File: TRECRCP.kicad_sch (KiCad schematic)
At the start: 44 parts, among them K1 12v Coil Relay, K2 12v Coil Relay, K5 Fujitsu_FTR-LYCA005x, K6 Fujitsu_FTR-LYCA005x, K7 Fujitsu_FTR-LYCA005x, Q2 STF40NF03L, Q3 STF40NF03L, Q4 STF40NF03L, SW1 Dispatch2, SW1 Maint/Off/On Switch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

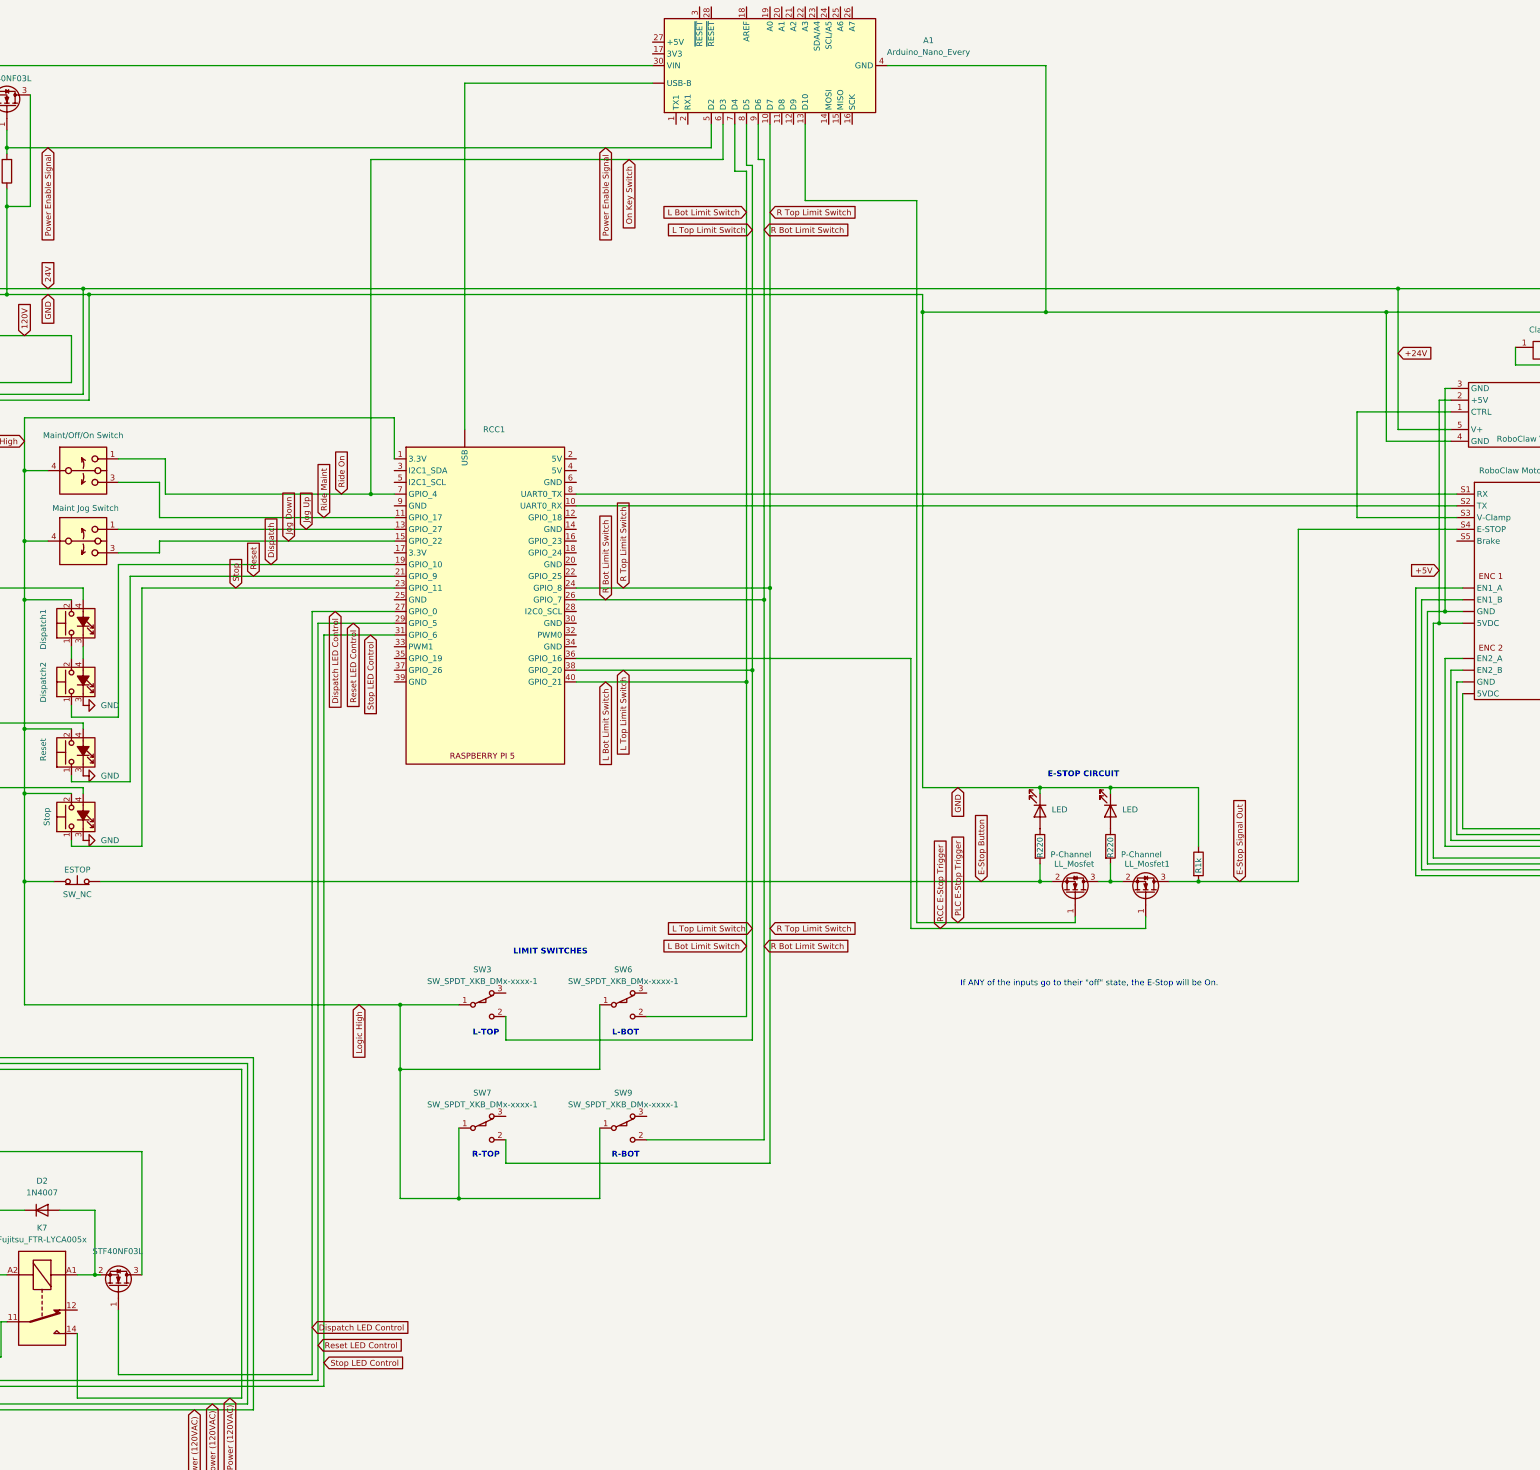
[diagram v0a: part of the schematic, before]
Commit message: Add Pi PSU
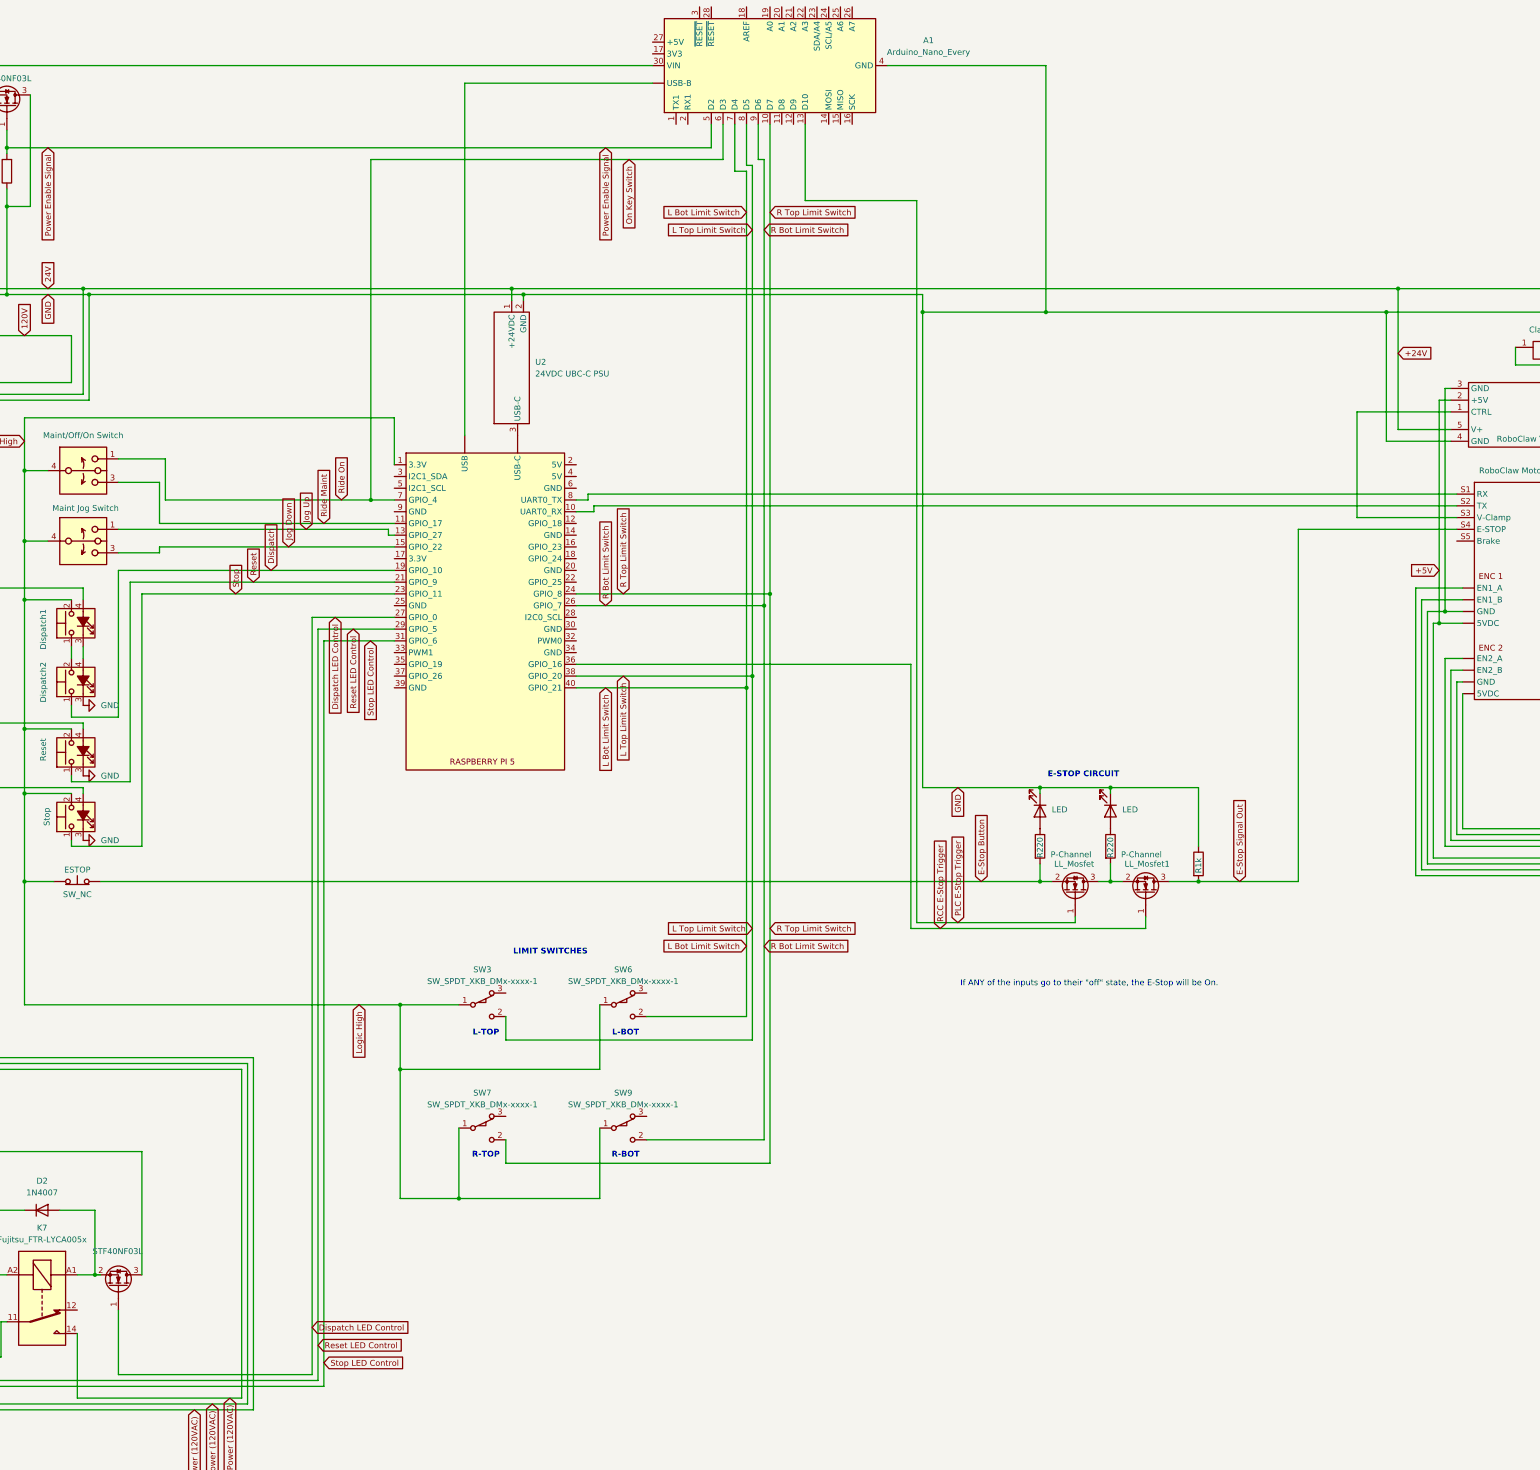
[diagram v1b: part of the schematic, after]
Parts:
- added U2: 24VDC UBC-C PSU, symbol custom symbols:Pi_PSU
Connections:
- net +24V: now also U2.1 (+24VDC)
- net GND: now also U2.2 (GND)
- new net: RCC1. (USB-C), U2.3 (USB-C)

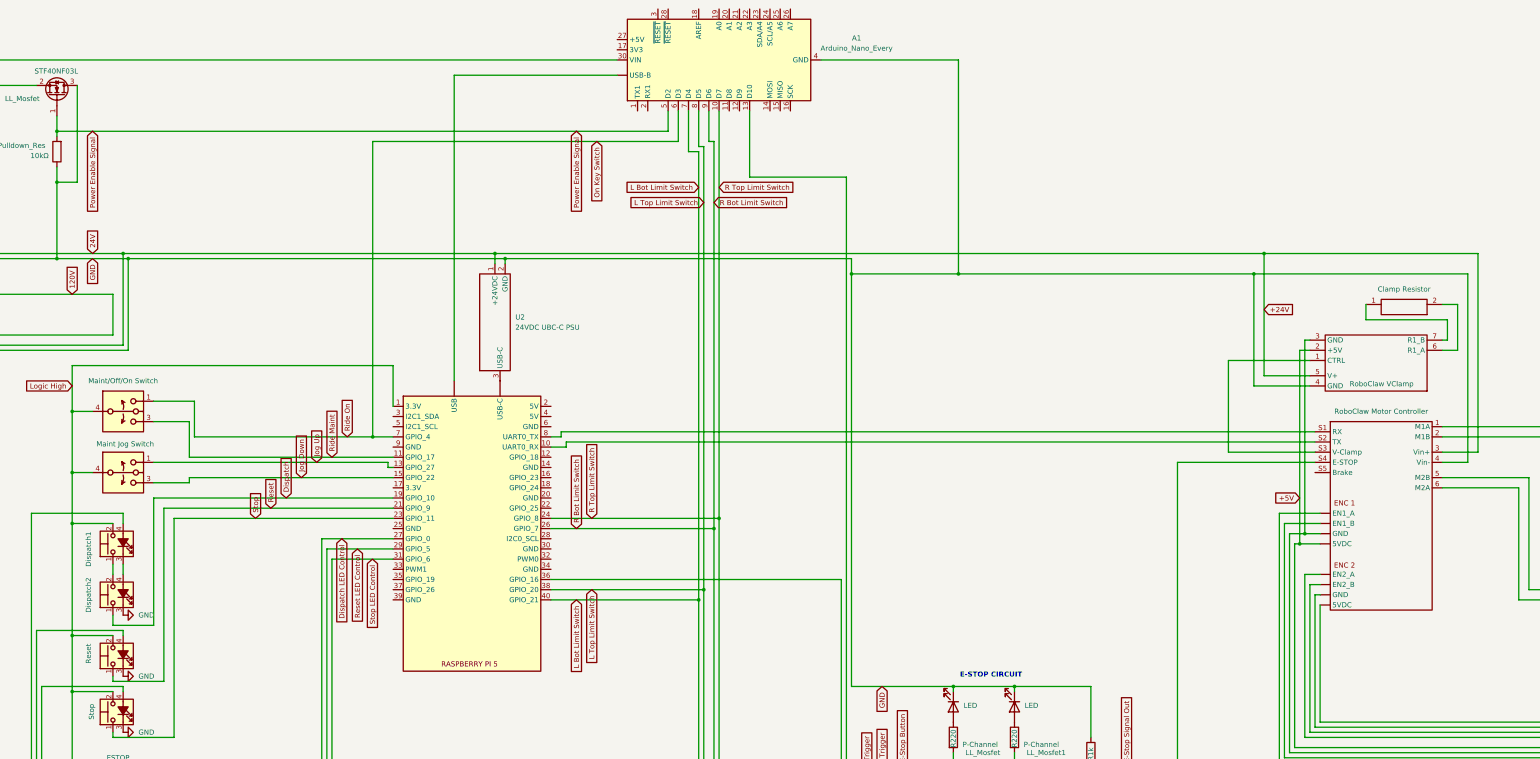
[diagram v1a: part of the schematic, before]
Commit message: Change RCP Logic High
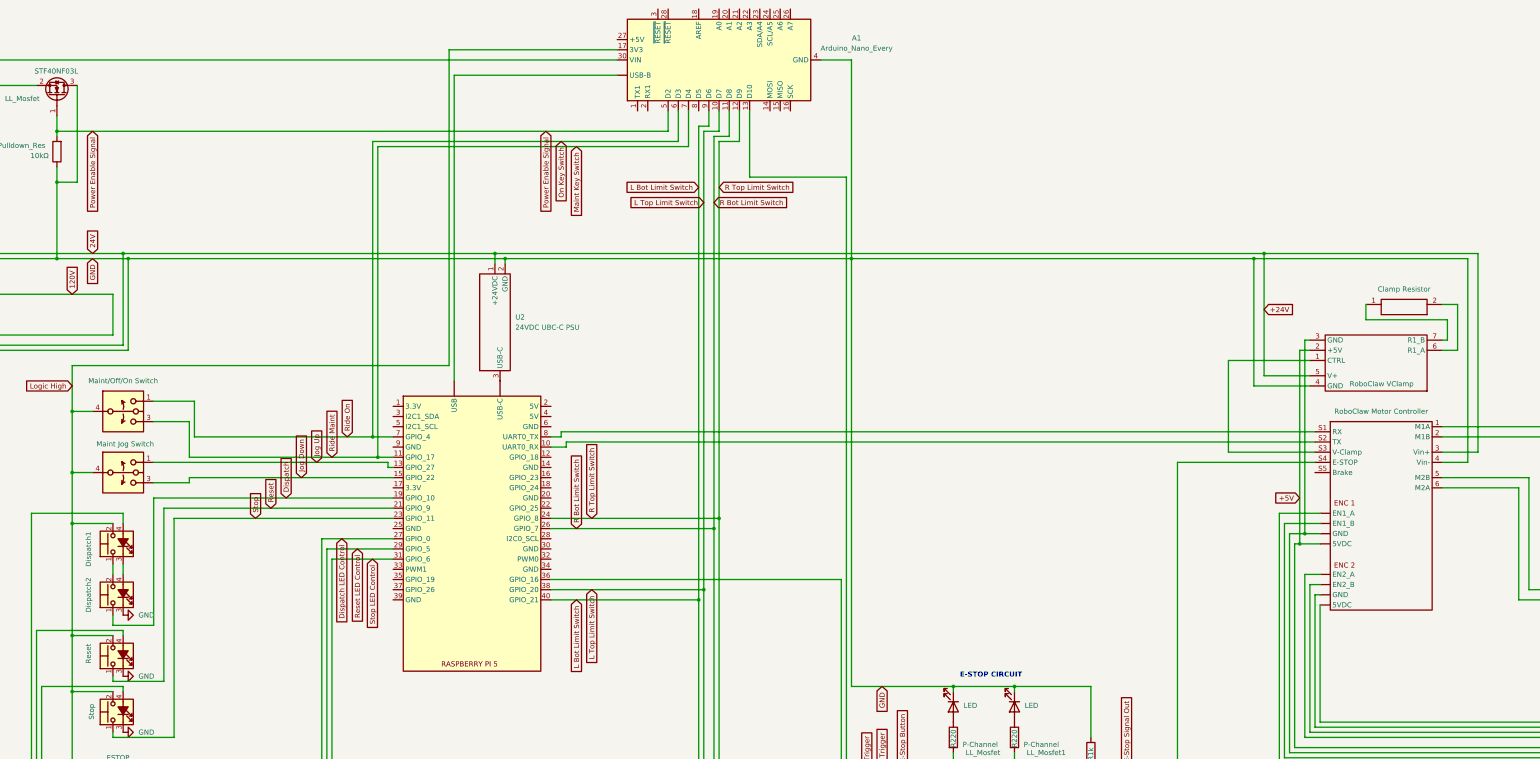
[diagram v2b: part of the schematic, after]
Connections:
- net L Bot Limit Switch: now also A1.9 (D6); no longer A1.7 (D4)
- net L Top Limit Switch: now also A1.10 (D7); no longer A1.8 (D5)
- net Logic High: now also A1.17 (3V3); no longer RCC1.1 (3.3V)
- net R Bot Limit Switch: now also A1.11 (D8); no longer A1.9 (D6)
- net R Top Limit Switch: now also A1.12 (D9); no longer A1.10 (D7)
- net Ride Maint renamed Maint Key Switch
- net Maint Key Switch: now also A1.7 (D4)

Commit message: changes
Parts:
- added U3: ~, symbol TREC SYMBOL LIB:TOUCHSCREEN
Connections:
- net GND: no longer SW1.3 (K), SW4.3 (K), SW8.3 (K)
- net Logic High: now also RCC1.1 (3.3V)
- net NEUT: now also SW1.3 (K), SW4.3 (K), SW8.3 (K)
- new net: RCC1. (USB-C), U3. (Micro_USB) (x2)
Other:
- note added: "Connector A - 14pin Molex"
- note added: "HDMI and USB Panel Connectors"
- note added: "RIDE CONTROL PANEL"
- moved on the sheet: ESTOP, Pulldown_Res
